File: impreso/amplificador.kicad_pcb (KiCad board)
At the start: 2 copper layers, 191.8 x 97.2 mm, 93 parts, among them Q1 MPSA92, Q10 MPSA42, Q11 MPSA42, Q1201 MPSA92, Q1202 MPSA92, Q14 MJE340, Q15 MJE350, Q1501 MPSA42, Q1502 MPSA42, Q16 MJE340, Q17 MJE350, Q18 2SC3281, Q19 2SC3281, Q2 MPSA92, Q20 2SA1302, Q21 2SA1302, Q3 MPSA42, Q4 MPSA42, Q501 MPSA92, Q502 MPSA92, Q701 MPSA92, Q702 MPSA92, Q801 MJE350, Q802 MJE340, T1 TORNILLO, T2 TORNILLO, T3 TORNILLO, T4 TORNILLO, T5 TORNILLO, T6 TORNILLO, T7 TORNILLO, T8 TORNILLO

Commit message: Esta casi listo el PCB, necesito ayuda, ensanchen las pistas de potencia, pongan un plano de masa atrás, para vincular todos los componentes que falta mandar a masa, y hacen falta un par de vías.
Con más tiempo, lo dejaría mejor, pero es un quilombo. Tendría que comparar como hice la vez pasada, que me quedó de re chupete.
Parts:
- removed C10, C11, C13, C14, C16, C17, C9: CP, Capacitors_Elko_ThroughHole:Elko_vert_11.5x8mm_RM3.5
- removed C12: CP, Capacitors_ThroughHole:C_Rect_L18_W5_P15
- removed C15, C8: C, Capacitors_Elko_ThroughHole:Elko_vert_11.5x8mm_RM3.5
- removed D10, D11: D, Diodes_ThroughHole:Diode_DO-35_SOD27_Horizontal_RM10
- removed D12: D, Diodes_ThroughHole:Diode_DO-41_SOD81_Horizontal_RM10
- removed D8, D9: ZENER, Diodes_ThroughHole:Diode_DO-35_SOD27_Horizontal_RM10
- removed JP6, JP7: JUMPER, Pin_Headers:Pin_Header_Straight_1x02
- removed Q1201, Q1202, Q501, Q502, Q701, Q702: MPSA92, Housings_TO-92:TO-92_Inline_Narrow_Oval
- removed Q1501, Q1502: MPSA42, Housings_TO-92:TO-92_Inline_Narrow_Oval
- removed Q17: MJE350, Housings_SOT:SOT126_SOT32_Housing_Vertical
- removed Q18, Q19: 2SC3281, bibliotecas:DT-25-B01W-03
- removed Q21: 2SA1302, bibliotecas:DT-25-B01W-03
- removed Q801: MJE350, bibliotecas:Bornera_Chica
- removed Q802: MJE340, bibliotecas:Bornera_Chica
- removed R20, R21, R22, R23, R25, R26, R28, R29, R30, R31, R32, R33, R34, R35, R36: R, Resistors_ThroughHole:Resistor_Horizontal_RM10mm
- removed R27: R, Resistors_ThroughHole:Resistor_Horizontal_RM20mm
- removed R37, R40: R, Resistors_ThroughHole:Resistor_Ceramic_Horizontal_L36mm-W11mm-H10mm-p45mm
- removed RV1: POT, Potentiometers:Potentiometer_Bourns_3296W_3-8Zoll_Inline_ScrewUp
- removed T1, T2: TORNILLO, bibliotecas:TORNILLO
- added C2: 47u, Capacitors_ThroughHole:C_Rect_L7_W3.5_P5, F.Cu at (21.6, 82.5)
- added C4: 220u, Discret:CP5, F.Cu at (227.3, 151.6)
- added C5: 220u, Discret:CP5, F.Cu at (125.5, 60.5)
- added C_comp_1: 40p, Discret:CP5, F.Cu at (85.1, 128.3)
- added C_comp_2: 40p, Discret:CP5, F.Cu at (85.1, 72.4)
- added C_comp_3: 4p, Capacitors_ThroughHole:C_Rect_L7_W3.5_P5, F.Cu at (68.6, 95.2)
- added C_mvbe_comp1: 20n, Discret:CP5, F.Cu at (99.3, 101.9)
- added D1: MBR1645, Diodes_ThroughHole:Diode_DO-41_SOD81_Horizontal_RM10, F.Cu at (129.5, 66.0)
- added D2: D1N4148, Diodes_ThroughHole:Diode_DO-35_SOD27_Horizontal_RM10, F.Cu at (106.7, 68.1)
- added D3: D1N746, Diodes_ThroughHole:Diode_DO-35_SOD27_Horizontal_RM10, F.Cu at (96.5, 72.9)
- added D4: D1N746, Diodes_ThroughHole:Diode_DO-35_SOD27_Horizontal_RM10, F.Cu at (106.7, 127.8)
- added D5: D1N4148, Diodes_ThroughHole:Diode_DO-35_SOD27_Horizontal_RM10, F.Cu at (96.5, 132.8)
- added D_1: LED, LEDs:LED-5MM, F.Cu at (44.5, 88.9)
- added D_2: LED, LEDs:LED-5MM, F.Cu at (47.0, 108.0)
- added Q12: 2SA1302, bibliotecas:DT-25-B01W-03, F.Cu at (224.0, 141.0)
- added Q13: MPSA92, TO_SOT_Packages_THT:TO-92_Horizontal1_Inline_Narrow_Oval, F.Cu at (73.7, 71.4)
- added Q6: MJE350, TO_SOT_Packages_THT:SOT126_SOT32_Housing_Vertical, F.Cu at (158.0, 133.1)
- added Q7: 2SA1302, bibliotecas:DT-25-B01W-03, F.Cu at (224.0, 99.3)
- added Q8: MJE350, TO_SOT_Packages_THT:SOT126_SOT32_Housing_Vertical, F.Cu at (114.3, 130.8)
- added Q9: MPSA42, TO_SOT_Packages_THT:TO-92_Horizontal1_Inline_Narrow_Oval, F.Cu at (76.2, 134.3)
- added R11: 10k, Resistors_ThroughHole:Resistor_Horizontal_RM10mm, F.Cu at (71.1, 101.6)
- added R12: 10k, Resistors_ThroughHole:Resistor_Horizontal_RM10mm, F.Cu at (26.7, 90.2)
- added R17: 0R1, Resistors_ThroughHole:Resistor_Ceramic_Horizontal_L36mm-W11mm-H10mm-p45mm, F.Cu at (209.0, 70.4)
- added R19: 150R, Resistors_ThroughHole:Resistor_Horizontal_RM10mm, F.Cu at (124.5, 78.5)
- added R2: 0R25, Resistors_ThroughHole:Resistor_Ceramic_Horizontal_L36mm-W11mm-H10mm-p45mm, F.Cu at (119.4, 88.9)
- added RC1: 2.4k, Resistors_ThroughHole:Resistor_Horizontal_RM10mm, F.Cu at (57.1, 67.3)
- added RC2: 2.4k, Resistors_ThroughHole:Resistor_Horizontal_RM10mm, F.Cu at (57.1, 133.3)
- added R_curr1: 820R, Resistors_ThroughHole:Resistor_Horizontal_RM10mm, F.Cu at (45.7, 95.2)
- added R_curr2: 820R, Resistors_ThroughHole:Resistor_Horizontal_RM10mm, F.Cu at (41.9, 114.3)
- added R_led1: 6.8k, Resistors_ThroughHole:Resistor_Horizontal_RM10mm, F.Cu at (35.6, 88.9)
- added R_led2: 6.8k, Resistors_ThroughHole:Resistor_Horizontal_RM10mm, F.Cu at (35.6, 108.0)
- added Rmvbe1: 270R, Resistors_ThroughHole:Resistor_Horizontal_RM10mm, F.Cu at (107.7, 105.9)
- added U1: MMPQ2222A, pcb:SOIC-16, F.Cu at (54.4, 81.9)
- added U2: MMPQ2907A, pcb:SOIC-16, F.Cu at (54.4, 117.5)
- added U3: LM7809CT, Power_Integrations:TO-220, F.Cu at (44.5, 72.4)
- added U4: LM7909CT, Power_Integrations:TO-220, F.Cu at (44.5, 128.3)
- C1: value C -> 1m; footprint Capacitors_Elko_ThroughHole:Elko_vert_11.5x8mm_RM3.5 -> Capacitors_ThroughHole:C_Rect_L7_W3.5_P5
- C3: value C -> 10n; footprint Capacitors_Elko_ThroughHole:Elko_vert_11.5x8mm_RM3.5 -> Capacitors_ThroughHole:C_Rect_L7_W3.5_P5
- C6, C7: value CP -> 220u; footprint Capacitors_Elko_ThroughHole:Elko_vert_11.5x8mm_RM3.5 -> Discret:CP5
- Q1: value MPSA92 -> 2SC3281; footprint Housings_TO-92:TO-92_Inline_Narrow_Oval -> bibliotecas:DT-25-B01W-03
- Q10: footprint Housings_TO-92:TO-92_Inline_Narrow_Oval -> TO_SOT_Packages_THT:TO-92_Horizontal1_Inline_Narrow_Oval
- Q11, Q4: value MPSA42 -> 2SC3281; footprint Housings_TO-92:TO-92_Inline_Narrow_Oval -> bibliotecas:DT-25-B01W-03
- Q14: value MJE340 -> MPSA92; footprint Housings_SOT:SOT126_SOT32_Housing_Vertical -> TO_SOT_Packages_THT:TO-92_Horizontal1_Inline_Narrow_Oval
- Q15: value MJE350 -> MJE340; footprint Housings_SOT:SOT126_SOT32_Housing_Vertical -> bibliotecas:Bornera_Chica
- Q16: value MJE340 -> MJE350; footprint Housings_SOT:SOT126_SOT32_Housing_Vertical -> bibliotecas:Bornera_Chica
- Q2: value MPSA92 -> MJE340; footprint Housings_TO-92:TO-92_Inline_Narrow_Oval -> TO_SOT_Packages_THT:SOT126_SOT32_Housing_Vertical
- Q3: value MPSA42 -> MJE340; footprint Housings_TO-92:TO-92_Inline_Narrow_Oval -> TO_SOT_Packages_THT:SOT126_SOT32_Housing_Vertical
- R1, R3, R5, R6, R7, R9: value R -> 100R
- R10: value R -> 366R
- R13, R8: value R -> 33R
- R14, R15, R16: value R -> 0R1; footprint Resistors_ThroughHole:Resistor_Horizontal_RM10mm -> Resistors_ThroughHole:Resistor_Ceramic_Horizontal_L36mm-W11mm-H10mm-p45mm
- R18: value R -> 150R
- R4: value R -> 0R25; footprint Resistors_ThroughHole:Resistor_Horizontal_RM10mm -> Resistors_ThroughHole:Resistor_Ceramic_Horizontal_L36mm-W11mm-H10mm-p45mm
- moved T4 154.0 mm to (111.0, 65.0)
- moved T7 153.5 mm to (110.7, 141.0)
- moved D13 135.3 mm to (119.6, 133.9), turned to 0 degrees
- moved Q14 129.7 mm to (76.2, 66.0), turned to 270 degrees
- moved C7 126.9 mm to (203.5, 50.0), turned to 0 degrees
- moved JP4 120.4 mm to (66.0, 138.4)
- moved T3 106.2 mm to (158.0, 59.7)
- moved JP3 99.9 mm to (64.8, 62.2)
- moved RV2 99.3 mm to (104.9, 98.8)
- moved Q1 95.5 mm to (197.1, 99.3), turned to 0 degrees
- moved Q15 92.6 mm to (137.2, 72.4), turned to 270 degrees
- moved R14 88.4 mm to (208.8, 129.3), turned to 0 degrees
- moved T6 86.7 mm to (87.4, 118.4)
- moved Q16 86.6 mm to (137.2, 128.8), turned to 270 degrees
- moved T5 86.6 mm to (87.6, 111.3)
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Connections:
- C1 pad 2: Entrada -> EntradaGND
- C6 pad 1: Net-(C6-Pad1) -> EntradaGND
- C6 pad 2: SalidaGND -> -15
- C7 pad 1: SalidaGND -> +50
- C7 pad 2: Net-(C10-Pad2) -> EntradaGND
- JP1 pad 1: Net-(C6-Pad1) -> Net-(JP1-Pad1)
- JP1 pad 2: Net-(JP1-Pad2) -> Net-(C_comp_2-Pad1)
- JP3 pad 2: Net-(JP3-Pad2) -> +50
- JP4 pad 1: Net-(JP1-Pad2) -> Net-(JP4-Pad1)
- JP4 pad 2: +50 -> -50
- JP5 pad 1: Net-(C9-Pad1) -> Net-(C_comp_3-Pad2)
- JP5 pad 2: Net-(JP5-Pad2) -> Realim
- Q1 pad 2: Net-(C1-Pad1) -> +50
- Q1 pad 3: Net-(JP2-Pad1) -> Net-(Q1-Pad3)
- Q10 pad 3: SalidaGND -> EntradaGND
- Q11 pad 1: Net-(Q11-Pad1) -> Net-(Q1-Pad1)
- Q11 pad 2: Net-(Q10-Pad1) -> +50
- Q11 pad 3: Net-(C9-Pad1) -> Net-(Q11-Pad3)
- Q14 pad 1: Net-(C15-Pad1) -> Net-(Q14-Pad1)
- Q14 pad 2: +50 -> Net-(Q13-Pad1)
- Q15 pad 1: Net-(C15-Pad2) -> Net-(Q15-Pad1)
- Q15 pad 2: -50 -> Net-(C_mvbe_comp1-Pad1)
- Q16 pad 1: Net-(Q16-Pad1) -> Net-(Q15-Pad1)
- Q16 pad 2: +50 -> Net-(C_mvbe_comp1-Pad2)
- Q16 pad 3: Net-(D10-Pad1) -> Net-(Q16-Pad3)
- Q2 pad 1: Net-(Q2-Pad1) -> Net-(Q1-Pad1)
- Q2 pad 2: Net-(Q2-Pad2) -> +50
- Q2 pad 3: Net-(Q2-Pad3) -> Net-(D2-Pad1)
- Q20 pad 1: Net-(C15-Pad2) -> Net-(C3-Pad2)
- Q3 pad 1: Net-(Q3-Pad1) -> Net-(C3-Pad1)
- Q3 pad 2: Net-(Q2-Pad3) -> +50
- Q3 pad 3: Net-(JP2-Pad1) -> Net-(Q3-Pad3)
- Q4 pad 1: Net-(Q4-Pad1) -> Net-(C3-Pad1)
- Q4 pad 2: Net-(Q2-Pad3) -> Net-(D1-Pad1)
- Q4 pad 3: Net-(Q2-Pad3) -> Net-(Q4-Pad3)
- R1 pad 1: Entrada -> Net-(Q1-Pad1)
- R1 pad 2: SalidaGND -> Net-(D1-Pad1)
- R10 pad 1: Net-(C6-Pad1) -> Net-(C_comp_3-Pad1)
- R10 pad 2: Net-(Q501-Pad1) -> Net-(C1-Pad1)
- R13 pad 1: Net-(Q501-Pad2) -> +50
- R13 pad 2: SalidaGND -> Net-(Q14-Pad1)
- R14 pad 1: Net-(Q701-Pad3) -> Net-(D13-Pad2)
- R14 pad 2: SalidaGND -> Net-(Q12-Pad3)
- R15 pad 1: Net-(Q2-Pad2) -> Net-(D13-Pad2)
- R16 pad 1: Net-(JP7-Pad1) -> Net-(Q1-Pad3)
- R16 pad 2: Net-(Q2-Pad2) -> Net-(D1-Pad1)
- R18 pad 1: Net-(JP1-Pad2) -> Net-(Q16-Pad3)
- R18 pad 2: Net-(Q701-Pad2) -> Net-(C_mvbe_comp1-Pad2)
- R3 pad 1: Net-(C1-Pad1) -> Net-(C3-Pad1)
- R3 pad 2: Net-(C3-Pad2) -> Realim
- R4 pad 1: Net-(C3-Pad2) -> Realim
- R4 pad 2: SalidaGND -> Net-(Q20-Pad3)
- R5 pad 1: Net-(Q501-Pad3) -> Net-(D13-Pad2)
- R5 pad 2: Net-(Q1-Pad1) -> Net-(Q12-Pad1)
- R6 pad 1: Net-(Q3-Pad1) -> Net-(Q3-Pad3)
- R6 pad 2: Net-(C10-Pad2) -> Net-(C_mvbe_comp1-Pad1)
- R7 pad 1: Net-(Q501-Pad3) -> Net-(Q6-Pad3)
- R7 pad 2: Net-(Q2-Pad1) -> Net-(C_mvbe_comp1-Pad2)
- R8 pad 1: Net-(Q4-Pad1) -> Net-(Q9-Pad1)
- R8 pad 2: Net-(C10-Pad2) -> -50
- R9 pad 1: Net-(Q2-Pad2) -> Realim
- R9 pad 2: Net-(C3-Pad1) -> Net-(C3-Pad2)
- RV2 pad 1: Net-(Q802-Pad3) -> Net-(Q15-Pad3)
- T5 pad 1: Salida -> Realim
- T6 pad 1: SalidaGND -> EntradaGND
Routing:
- net Net-(Q12-Pad1): track 0.00 -> 152.7 mm
- net Net-(Q1-Pad1): track 3.81 -> 123.6 mm
- net Salida: track 116.3 -> 0.00 mm
- net Net-(D_1-Pad1): track 0.00 -> 94.1 mm
- net Realim: track 0.00 -> 85.2 mm
- net Net-(D1-Pad1): track 0.00 -> 85.1 mm
- net Net-(Q15-Pad1): track 0.00 -> 76.0 mm
- net +15: track 15.2 -> 90.7 mm
- net -15: track 16.5 -> 89.9 mm
- net -50: track 169.7 -> 237.8 mm
- net Net-(C2-Pad1): track 0.00 -> 66.1 mm
- net Net-(C15-Pad2): track 65.3 -> 0.00 mm
- net Net-(D_2-Pad2): track 0.00 -> 65.2 mm
- net Net-(C_mvbe_comp1-Pad2): track 0.00 -> 64.7 mm
- net Net-(C_mvbe_comp1-Pad1): track 0.00 -> 64.6 mm
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- removed copper zone on F.Cu, net SalidaGND
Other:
- board outline removed
- board text removed: "CE2 Grupo 5"

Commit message: Terminé la versión 0.1 del PCB. Listo? Aprobamos el informe de avance?
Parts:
- moved Q14 2.05 mm to (76.5, 68.1), turned to 0 degrees
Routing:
- net Net-(Q15-Pad1): track 76.0 -> 0.00 mm
- net (no net): track 0.00 -> 76.0 mm
- net Net-(C3-Pad1): track 24.5 -> 87.2 mm, vias 0 -> 2
- net Net-(C_comp_3-Pad1): track 30.3 -> 76.8 mm, vias 0 -> 4
- net +50: track 190.7 -> 217.8 mm, vias 0 -> 1
- net Net-(Q16-Pad3): track 34.0 -> 51.3 mm, vias 0 -> 2
- net Net-(C2-Pad1): track 66.1 -> 82.8 mm, vias 0 -> 2
- net -50: track 237.8 -> 253.3 mm, vias 0 -> 2
- net Net-(Q13-Pad1): track 0.00 -> 5.76 mm
- net Realim: track 85.2 -> 80.7 mm
- net Net-(C_comp_2-Pad2): track 27.1 -> 24.9 mm
- net Net-(C3-Pad2): track 63.4 -> 64.6 mm
- net Net-(D_1-Pad1): track 94.1 -> 95.1 mm
- net Net-(Q14-Pad1): track 5.08 -> 5.62 mm
- net EntradaGND: vias 0 -> 1
- added copper zone on B.Cu, net EntradaGND

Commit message: Agregué la Red de Zobel.
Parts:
- added Czobel1: 100n, Capacitors_ThroughHole:C_Rect_L7_W3.5_P5, F.Cu at (76.3, 83.3)
- added Rzobel1: 10R, Resistors_ThroughHole:Resistor_Horizontal_RM10mm, F.Cu at (91.4, 83.3)
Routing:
- net Realim: track 80.7 -> 86.3 mm
- net Net-(Czobel1-Pad2): track 0.00 -> 5.08 mm
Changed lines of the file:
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@@
 (kicad_pcb (version 4) (host pcbnew 0.201512080931+6353~38~ubuntu14.04.1-stable)
   (general
-    (links 140)
-    (no_connects 47)
-    (area 15.114999 47.337999 236.495001 154.628)
+    (links 143)
+    (no_connects 37)
+    (area 0 0 0 0)
     (thickness 1.6)
     (drawings 0)
-    (tracks 362)
+    (tracks 364)
     (zones 0)
-    (modules 77)
-    (nets 56)
+    (modules 79)
+    (nets 57)
   )
   (page A4)
@@
   (net 54 Entrada)
   (net 55 "Net-(R_curr2-Pad2)")
+  (net 56 "Net-(Czobel1-Pad2)")
   (net_class Default "This is the default net class."
     (clearance 0.2)
@@
     (add_net "Net-(C_mvbe_comp1-Pad1)")
     (add_net "Net-(C_mvbe_comp1-Pad2)")
+    (add_net "Net-(Czobel1-Pad2)")
     (add_net "Net-(D1-Pad1)")
     (add_net "Net-(D13-Pad2)")
@@
     (pad 1 thru_hole oval (at -2.54 0) (size 2.032 2.54) (drill 1.143) (layers *.Cu *.Mask F.SilkS)
       (net 2 EntradaGND))
+  )
+  (module Capacitors_ThroughHole:C_Rect_L7_W3.5_P5 (layer F.Cu)
+    (at 76.28 83.312)
+    (descr "Film Capacitor Length 7mm x Width 3.5mm, Pitch 5mm")
+    (tags Capacitor)
+    (fp_text reference Czobel1 (at 2.5 -3) (layer F.SilkS)
+      (effects (font (size 1 1) (thickness 0.15)))
+    )
+    (fp_text value 100n (at 2.5 3) (layer F.Fab)
+      (effects (font (size 1 1) (thickness 0.15)))
+    )
+    (fp_line (start -1.25 -2) (end 6.25 -2) (layer F.CrtYd) (width 0.05))
+    (fp_line (start 6.25 -2) (end 6.25 2) (layer F.CrtYd) (width 0.05))
+    (fp_line (start 6.25 2) (end -1.25 2) (layer F.CrtYd) (width 0.05))
+    (fp_line (start -1.25 2) (end -1.25 -2) (layer F.CrtYd) (width 0.05))
+    (fp_line (start -1 -1.75) (end 6 -1.75) (layer F.SilkS) (width 0.15))
+    (fp_line (start 6 -1.75) (end 6 1.75) (layer F.SilkS) (width 0.15))
+    (fp_line (start 6 1.75) (end -1 1.75) (layer F.SilkS) (width 0.15))
+    (fp_line (start -1 1.75) (end -1 -1.75) (layer F.SilkS) (width 0.15))
+    (pad 1 thru_hole rect (at 0 0) (size 1.3 1.3) (drill 0.8) (layers *.Cu *.Mask F.SilkS)
+      (net 2 EntradaGND))
+    (pad 2 thru_hole circle (at 5 0) (size 1.3 1.3) (drill 0.8) (layers *.Cu *.Mask F.SilkS)
+      (net 56 "Net-(Czobel1-Pad2)"))
+  )
+  (module Resistors_ThroughHole:Resistor_Horizontal_RM10mm (layer F.Cu)
+    (at 91.44 83.312 180)
+    (descr "Resistor, Axial,  RM 10mm, 1/3W,")
+    (tags "Resistor, Axial, RM 10mm, 1/3W,")
+    (fp_text reference Rzobel1 (at 0.24892 -3.50012 180) (layer F.SilkS)
+      (effects (font (size 1 1) (thickness 0.15)))
+    )
+    (fp_text value 10R (at 3.81 3.81 180) (layer F.Fab)
+      (effects (font (size 1 1) (thickness 0.15)))
+    )
+    (fp_line (start -2.54 -1.27) (end 2.54 -1.27) (layer F.SilkS) (width 0.15))
+    (fp_line (start 2.54 -1.27) (end 2.54 1.27) (layer F.SilkS) (width 0.15))
+    (fp_line (start 2.54 1.27) (end -2.54 1.27) (layer F.SilkS) (width 0.15))
+    (fp_line (start -2.54 1.27) (end -2.54 -1.27) (layer F.SilkS) (width 0.15))
+    (fp_line (start -2.54 0) (end -3.81 0) (layer F.SilkS) (width 0.15))
+    (fp_line (start 2.54 0) (end 3.81 0) (layer F.SilkS) (width 0.15))
+    (pad 1 thru_hole circle (at -5.08 0 180) (size 1.99898 1.99898) (drill 1.00076) (layers *.Cu *.SilkS *.Mask)
+      (net 30 Realim))
+    (pad 2 thru_hole circle (at 5.08 0 180) (size 1.99898 1.99898) (drill 1.00076) (layers *.Cu *.SilkS *.Mask)
+      (net 56 "Net-(Czobel1-Pad2)"))
+    (model Resistors_ThroughHole.3dshapes/Resistor_Horizontal_RM10mm.wrl
+      (at (xyz 0 0 0))
+      (scale (xyz 0.4 0.4 0.4))
+      (rotate (xyz 0 0 0))
+    )
   )
   (segment (start 137.16 123.878) (end 135.745787 123.878) (width 0.9) (layer F.Cu) (net 0))
@@
   (segment (start 57.15 62.23) (end 64.77 62.23) (width 0.9) (layer F.Cu) (net 28))
   (segment (start 57.15 138.43) (end 66.04 138.43) (width 0.9) (layer F.Cu) (net 29))
+  (segment (start 96.52 83.312) (end 96.52 88.9) (width 0.9) (layer F.Cu) (net 30))
   (segment (start 96.52 114.3) (end 96.52 113.002002) (width 5) (layer F.Cu) (net 30))
   (segment (start 96.52 113.002002) (end 89.929999 106.412001) (width 5) (layer F.Cu) (net 30))
@@
   (segment (start 52.650002 119.38) (end 53.34 118.690002) (width 0.9) (layer F.Cu) (net 53))
   (segment (start 46.99 114.3) (end 51.55 114.3) (width 0.9) (layer F.Cu) (net 55))
+  (segment (start 81.28 83.312) (end 86.36 83.312) (width 0.9) (layer F.Cu) (net 56))
   (zone (net 2) (net_name EntradaGND) (layer B.Cu) (hatch edge 0.508)
     (connect_pads (clearance 0.508))

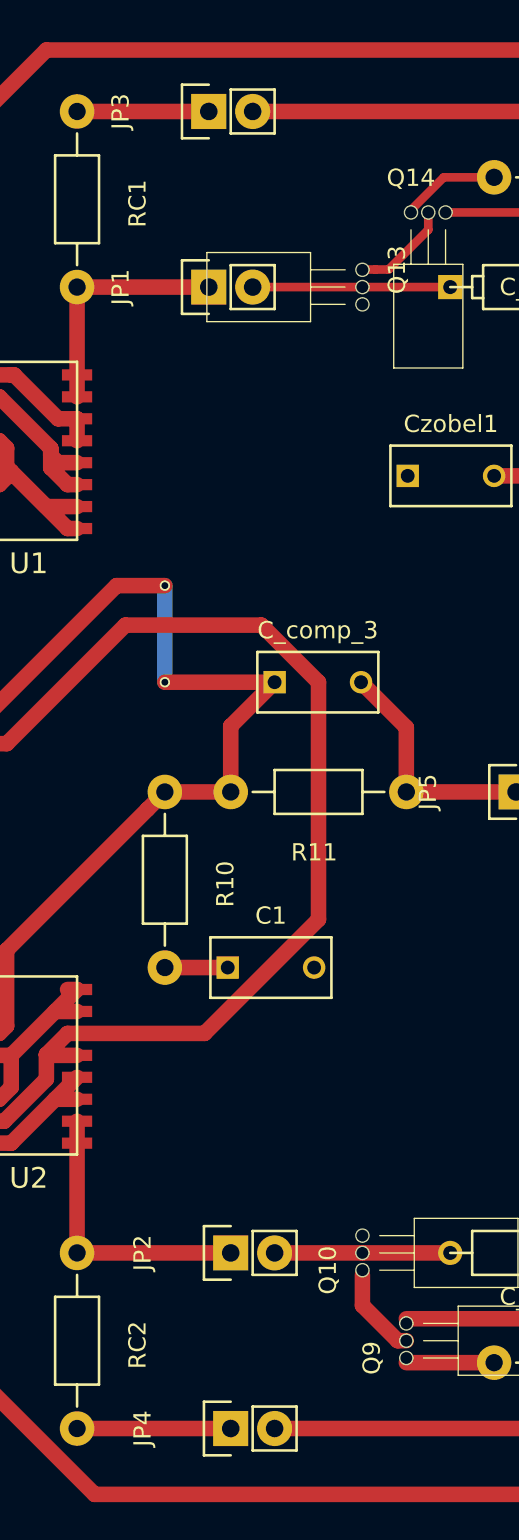
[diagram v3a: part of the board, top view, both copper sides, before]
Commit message: Agregué resistencias de emisor, y resistencia a la salida. No pude agregar inductor, no lo encuentro en las bibliotecas.
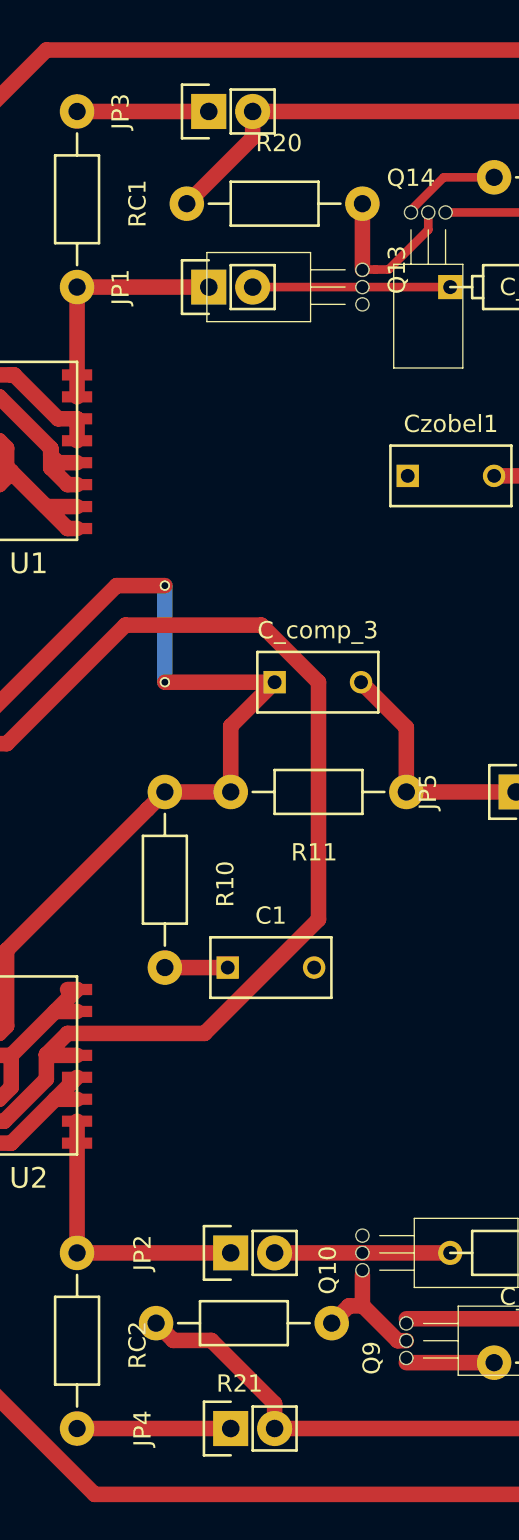
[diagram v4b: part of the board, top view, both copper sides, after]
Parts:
- added R20: 1K, Resistors_ThroughHole:Resistor_Horizontal_RM10mm, F.Cu at (68.6, 67.6)
- added R21: 1K, Resistors_ThroughHole:Resistor_Horizontal_RM10mm, F.Cu at (66.8, 132.3)
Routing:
- net -50: track 253.3 -> 263.5 mm
- net +50: track 217.8 -> 224.7 mm
- net Net-(Q13-Pad1): track 5.76 -> 9.57 mm
- net Net-(Q10-Pad1): track 5.15 -> 7.36 mm
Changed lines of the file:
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@@
 (kicad_pcb (version 4) (host pcbnew 0.201512080931+6353~38~ubuntu14.04.1-stable)
   (general
-    (links 143)
-    (no_connects 37)
+    (links 147)
+    (no_connects 39)
     (area 0 0 0 0)
     (thickness 1.6)
     (drawings 0)
-    (tracks 364)
+    (tracks 374)
     (zones 0)
-    (modules 79)
+    (modules 81)
     (nets 57)
   )
@@
     )
   )
+  (module Resistors_ThroughHole:Resistor_Horizontal_RM10mm (layer F.Cu)
+    (at 68.58 67.564)
+    (descr "Resistor, Axial,  RM 10mm, 1/3W,")
+    (tags "Resistor, Axial, RM 10mm, 1/3W,")
+    (fp_text reference R20 (at 0.24892 -3.50012) (layer F.SilkS)
+      (effects (font (size 1 1) (thickness 0.15)))
+    )
+    (fp_text value 1K (at 3.81 3.81) (layer F.Fab)
+      (effects (font (size 1 1) (thickness 0.15)))
+    )
+    (fp_line (start -2.54 -1.27) (end 2.54 -1.27) (layer F.SilkS) (width 0.15))
+    (fp_line (start 2.54 -1.27) (end 2.54 1.27) (layer F.SilkS) (width 0.15))
+    (fp_line (start 2.54 1.27) (end -2.54 1.27) (layer F.SilkS) (width 0.15))
+    (fp_line (start -2.54 1.27) (end -2.54 -1.27) (layer F.SilkS) (width 0.15))
+    (fp_line (start -2.54 0) (end -3.81 0) (layer F.SilkS) (width 0.15))
+    (fp_line (start 2.54 0) (end 3.81 0) (layer F.SilkS) (width 0.15))
+    (pad 1 thru_hole circle (at -5.08 0) (size 1.99898 1.99898) (drill 1.00076) (layers *.Cu *.SilkS *.Mask)
+      (net 9 +50))
+    (pad 2 thru_hole circle (at 5.08 0) (size 1.99898 1.99898) (drill 1.00076) (layers *.Cu *.SilkS *.Mask)
+      (net 42 "Net-(Q13-Pad1)"))
+    (model Resistors_ThroughHole.3dshapes/Resistor_Horizontal_RM10mm.wrl
+      (at (xyz 0 0 0))
+      (scale (xyz 0.4 0.4 0.4))
+      (rotate (xyz 0 0 0))
+    )
+  )
+  (module Resistors_ThroughHole:Resistor_Horizontal_RM10mm (layer F.Cu)
+    (at 66.802 132.334 180)
+    (descr "Resistor, Axial,  RM 10mm, 1/3W,")
+    (tags "Resistor, Axial, RM 10mm, 1/3W,")
+    (fp_text reference R21 (at 0.24892 -3.50012 180) (layer F.SilkS)
+      (effects (font (size 1 1) (thickness 0.15)))
+    )
+    (fp_text value 1K (at 3.81 3.81 180) (layer F.Fab)
+      (effects (font (size 1 1) (thickness 0.15)))
+    )
+    (fp_line (start -2.54 -1.27) (end 2.54 -1.27) (layer F.SilkS) (width 0.15))
+    (fp_line (start 2.54 -1.27) (end 2.54 1.27) (layer F.SilkS) (width 0.15))
+    (fp_line (start 2.54 1.27) (end -2.54 1.27) (layer F.SilkS) (width 0.15))
+    (fp_line (start -2.54 1.27) (end -2.54 -1.27) (layer F.SilkS) (width 0.15))
+    (fp_line (start -2.54 0) (end -3.81 0) (layer F.SilkS) (width 0.15))
+    (fp_line (start 2.54 0) (end 3.81 0) (layer F.SilkS) (width 0.15))
+    (pad 1 thru_hole circle (at -5.08 0 180) (size 1.99898 1.99898) (drill 1.00076) (layers *.Cu *.SilkS *.Mask)
+      (net 38 "Net-(Q10-Pad1)"))
+    (pad 2 thru_hole circle (at 5.08 0 180) (size 1.99898 1.99898) (drill 1.00076) (layers *.Cu *.SilkS *.Mask)
+      (net 6 -50))
+    (model Resistors_ThroughHole.3dshapes/Resistor_Horizontal_RM10mm.wrl
+      (at (xyz 0 0 0))
+      (scale (xyz 0.4 0.4 0.4))
+      (rotate (xyz 0 0 0))
+    )
+  )
   (segment (start 137.16 123.878) (end 135.745787 123.878) (width 0.9) (layer F.Cu) (net 0))
   (segment (start 137.004752 86.868) (end 137.16 86.868) (width 0.9) (layer F.Cu) (net 0))
@@
   (segment (start 128.778 105.156) (end 132.842 105.156) (width 0.9) (layer F.Cu) (net 5))
   (segment (start 132.842 105.156) (end 134.366 103.632) (width 0.9) (layer F.Cu) (net 5))
+  (segment (start 61.722 132.334) (end 62.721489 133.333489) (width 0.9) (layer F.Cu) (net 6))
+  (segment (start 62.721489 133.333489) (end 64.920329 133.333489) (width 0.9) (layer F.Cu) (net 6))
+  (segment (start 64.920329 133.333489) (end 68.58 136.99316) (width 0.9) (layer F.Cu) (net 6))
+  (segment (start 68.58 136.99316) (end 68.58 138.43) (width 0.9) (layer F.Cu) (net 6))
   (segment (start 166.624 133.096) (end 166.624 142.748) (width 0.5) (layer B.Cu) (net 6))
   (segment (start 157.988 133.096) (end 166.624 133.096) (width 0.5) (layer F.Cu) (net 6))
@@
   (segment (start 58.166 142.24) (end 44.45 128.524) (width 0.9) (layer F.Cu) (net 8))
   (segment (start 44.45 128.524) (end 44.45 128.27) (width 0.9) (layer F.Cu) (net 8))
+  (segment (start 63.5 67.564) (end 67.31 63.754) (width 0.9) (layer F.Cu) (net 9))
+  (segment (start 67.31 63.754) (end 67.31 62.23) (width 0.9) (layer F.Cu) (net 9))
   (segment (start 158.291309 60.706) (end 165.1 60.706) (width 0.5) (layer F.Cu) (net 9))
   (segment (start 157.988 57.15) (end 157.988 60.402691) (width 0.5) (layer F.Cu) (net 9))
@@
   (segment (start 114.332 128.778) (end 114.3 128.81) (width 0.9) (layer F.Cu) (net 36))
   (segment (start 231.648 112.522) (end 231.648 99.314) (width 5) (layer F.Cu) (net 37))
+  (segment (start 71.882 132.334) (end 72.881489 131.334511) (width 0.9) (layer F.Cu) (net 38))
+  (segment (start 72.881489 131.334511) (end 73.635489 131.334511) (width 0.9) (layer F.Cu) (net 38))
+  (segment (start 73.635489 131.334511) (end 73.66 131.31) (width 0.9) (layer F.Cu) (net 38))
   (segment (start 73.66 131.31) (end 73.66 129.54) (width 0.9) (layer F.Cu) (net 38))
   (segment (start 76.2 133.35) (end 75.7 133.35) (width 0.9) (layer F.Cu) (net 38))
@@
   (segment (start 217.932 70.358) (end 204.724 57.15) (width 5) (layer F.Cu) (net 40))
   (segment (start 231.648 129.286) (end 231.648 140.97) (width 5) (layer F.Cu) (net 41))
+  (segment (start 73.66 71.374) (end 73.66 67.564) (width 0.9) (layer F.Cu) (net 42))
   (segment (start 74.422 71.374) (end 73.66 71.374) (width 0.5) (layer F.Cu) (net 42))
   (segment (start 75.168 71.374) (end 74.422 71.374) (width 0.5) (layer F.Cu) (net 42))
